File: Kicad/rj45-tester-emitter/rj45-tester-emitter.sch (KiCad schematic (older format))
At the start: 25 parts

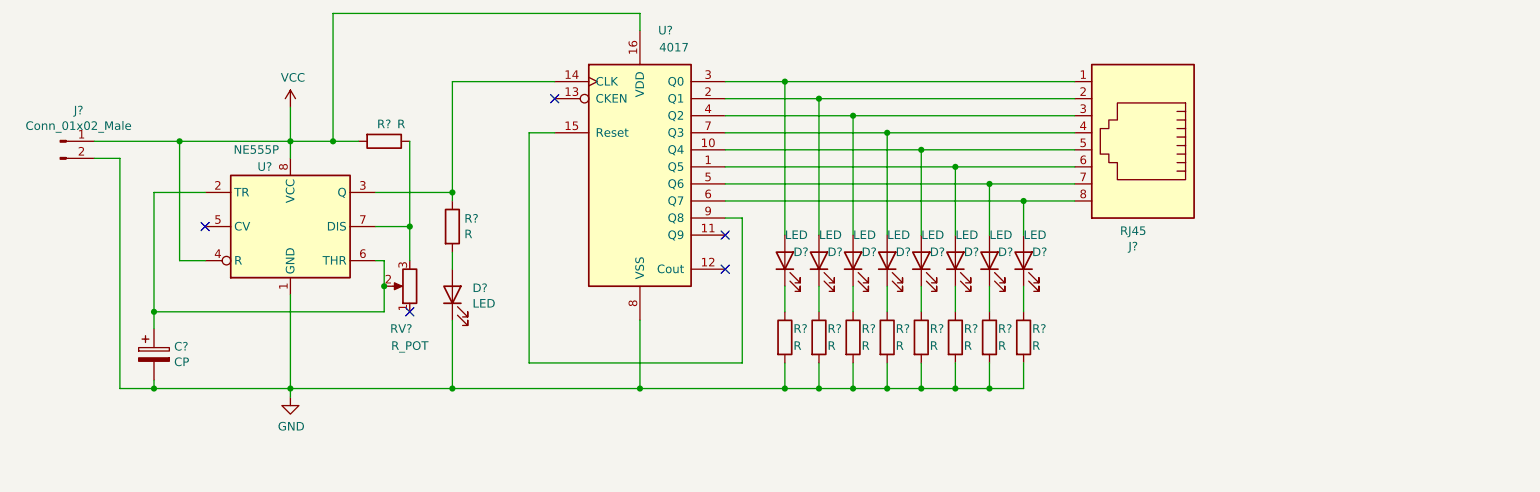
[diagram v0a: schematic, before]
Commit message: Add switch + bypass capacitor
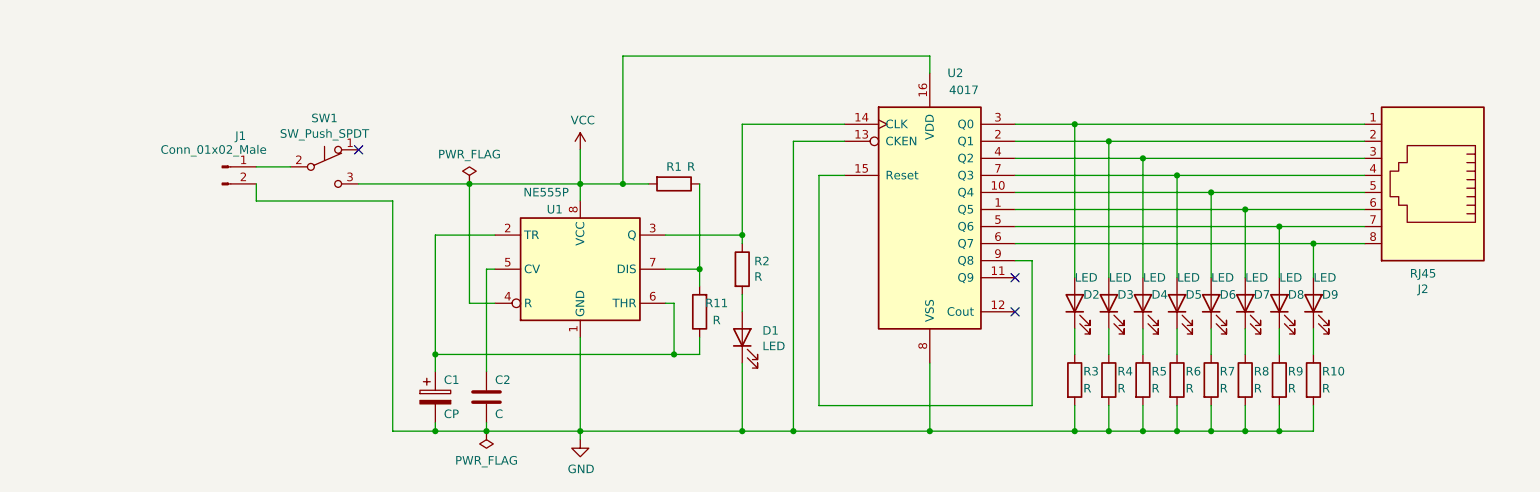
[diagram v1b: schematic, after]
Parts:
- removed RV?: R_POT, symbol Device:R_POT
- added C2: C, Capacitor_SMD:C_0805_2012Metric_Pad1.15x1.40mm_HandSolder, symbol Device:C
- added R11: R, Resistor_SMD:R_0805_2012Metric_Pad1.15x1.40mm_HandSolder, symbol Device:R
- added SW1: SW_Push_SPDT, symbol Switch:SW_Push_SPDT
- C1: renamed from C?; footprint (none) -> Capacitor_SMD:CP_Elec_6.3x5.2
- D1, D2, D3, D4, D5, D6, D7, D8, D9: renamed from D?; footprint (none) -> LED_SMD:LED_0805_2012Metric_Pad1.15x1.40mm_HandSolder
- J1: renamed from J?; footprint (none) -> Connector_JST:JST_XH_B2B-XH-A_1x02_P2.50mm_Vertical
- R1, R10, R2, R3, R4, R5, R6, R7, R8, R9: renamed from R?; footprint (none) -> Resistor_SMD:R_0805_2012Metric_Pad1.15x1.40mm_HandSolder
- U1: renamed from U?; footprint Package_DIP:DIP-8_W7.62mm -> Package_DIP:DIP-8_W8.89mm_SMDSocket_LongPads
- U2: renamed from U?; footprint (none) -> Package_DIP:DIP-16_W8.89mm_SMDSocket_LongPads
- gave numbers to parts that had none: 1
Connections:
- net GND: now also U2.13 (CKEN), C2.2
- net VCC: now also SW1.3 (C); no longer J1.1 (Pin_1)
- net at C1.1, U1.2 (TR), U1.6 (THR): now also R11.1
- net at U1.5 (CV): now also C2.1
- net at R1.1, U1.7 (DIS): now also R11.2
- new net: J1.1 (Pin_1), SW1.2 (B)
- no-connect marks 5 -> 3
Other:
- moved on the sheet: C1, D1, D2, D3, D4, D5, D6, D7, D8, D9, J1, J2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

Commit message: PCB finished
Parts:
- C1: value CP -> 47u; footprint Capacitor_SMD:CP_Elec_6.3x5.2 -> Capacitor_SMD:CP_Elec_5x5.3
- C2: value C -> 10u
- J2: footprint (none) -> Connector_RJ:RJ45_Amphenol_54602-x08_Horizontal
- R1, R11: value R -> 10K
- SW1: footprint (none) -> Connector_PinHeader_2.54mm:PinHeader_1x03_P2.54mm_Vertical
- U1: footprint Package_DIP:DIP-8_W8.89mm_SMDSocket_LongPads -> Package_SO:SOIC-8_3.9x4.9mm_P1.27mm
- U2: footprint Package_DIP:DIP-16_W8.89mm_SMDSocket_LongPads -> Package_SO:SOIC-16_3.9x9.9mm_P1.27mm
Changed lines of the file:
@@
 F 0 "U1" H 4000 3300 50  0000 C CNN
 F 1 "NE555P" H 3950 3400 50  0000 C CNN
-F 2 "Package_DIP:DIP-8_W8.89mm_SMDSocket_LongPads" H 4800 2550 50  0001 C CNN
+F 2 "Package_SO:SOIC-8_3.9x4.9mm_P1.27mm" H 4800 2550 50  0001 C CNN
 F 3 "http://www.ti.com/lit/ds/symlink/ne555.pdf" H 5000 2550 50  0001 C CNN
 	1    4150 2950
@@
 F 0 "U2" H 6350 3400 50  0000 C CNN
 F 1 "4017" H 6400 3300 50  0000 C CNN
-F 2 "Package_DIP:DIP-16_W8.89mm_SMDSocket_LongPads" H 6200 2600 50  0001 C CNN
+F 2 "Package_SO:SOIC-16_3.9x9.9mm_P1.27mm" H 6200 2600 50  0001 C CNN
 F 3 "http://www.intersil.com/content/dam/Intersil/documents/cd40/cd4017bms-22bms.pdf" H 6200 2600 50  0001 C CNN
 	1    6200 2600
@@
 $EndComp
 $Comp
-L Device:CP C1
-U 1 1 5F59578D
-P 3300 3700
-F 0 "C1" H 3350 3800 50  0000 L CNN
-F 1 "CP" H 3350 3600 50  0000 L CNN
-F 2 "Capacitor_SMD:CP_Elec_6.3x5.2" H 3338 3550 50  0001 C CNN
-F 3 "~" H 3300 3700 50  0001 C CNN
-	1    3300 3700
-	1    0    0    -1
-$EndComp
-$Comp
 L Device:LED D1
 U 1 1 5F595BD7
@@
 	0    -1   -1   0
 $EndComp
-$Comp
-L Connector:RJ45 J2
-U 1 1 5F596C3D
-P 9150 2400
-F 0 "J2" H 9207 3067 50  0000 C CNN
-F 1 "RJ45" H 9207 2976 50  0000 C CNN
-F 2 "" V 9150 2425 50  0001 C CNN
-F 3 "~" V 9150 2425 50  0001 C CNN
-	1    9150 2400
-	-1   0    0    1
-$EndComp
 Wire Wire Line
 	3650 3150 3500 3150
@@
 P 4700 2450
 F 0 "R1" V 4600 2450 50  0000 C CNN
-F 1 "R" V 4600 2550 50  0000 C CNN
+F 1 "10K" V 4600 2600 50  0000 C CNN
 F 2 "Resistor_SMD:R_0805_2012Metric_Pad1.15x1.40mm_HandSolder" V 4630 2450 50  0001 C CNN
 F 3 "~" H 4700 2450 50  0001 C CNN
@@
 P 3600 3700
 F 0 "C2" H 3650 3800 50  0000 L CNN
-F 1 "C" H 3650 3600 50  0000 L CNN
+F 1 "10u" H 3650 3600 50  0000 L CNN
 F 2 "Capacitor_SMD:C_0805_2012Metric_Pad1.15x1.40mm_HandSolder" H 3638 3550 50  0001 C CNN
 F 3 "~" H 3600 3700 50  0001 C CNN
@@
 F 0 "SW1" H 2650 2635 50  0000 C CNN
 F 1 "SW_Push_SPDT" H 2650 2544 50  0000 C CNN
-F 2 "" H 2650 2350 50  0001 C CNN
+F 2 "Connector_PinHeader_2.54mm:PinHeader_1x03_P2.54mm_Vertical" H 2650 2350 50  0001 C CNN
 F 3 "~" H 2650 2350 50  0001 C CNN
 	1    2650 2350
@@
 U 1 1 5F62B489
 P 4850 3200
-F 0 "R11" H 4750 3150 50  0000 C CNN
-F 1 "R" H 4750 3250 50  0000 C CNN
+F 0 "R11" H 4700 3150 50  0000 C CNN
+F 1 "10K" H 4700 3250 50  0000 C CNN
 F 2 "Resistor_SMD:R_0805_2012Metric_Pad1.15x1.40mm_HandSolder" V 4780 3200 50  0001 C CNN
 F 3 "~" H 4850 3200 50  0001 C CNN
@@
 	4850 3050 4850 2950
 Connection ~ 4850 2950
+$Comp
+L Connector:RJ45 J2
+U 1 1 5F5F9609
+P 9150 2400
+F 0 "J2" H 8820 2404 50  0000 R CNN
+F 1 "RJ45" H 8820 2495 50  0000 R CNN
+F 2 "Connector_RJ:RJ45_Amphenol_54602-x08_Horizontal" V 9150 2425 50  0001 C CNN
+F 3 "~" V 9150 2425 50  0001 C CNN
+	1    9150 2400
+	-1   0    0    1
+$EndComp
+$Comp
+L Device:CP C1
+U 1 1 5F59578D
+P 3300 3700
+F 0 "C1" H 3350 3800 50  0000 L CNN
+F 1 "47u" H 3350 3600 50  0000 L CNN
+F 2 "Capacitor_SMD:CP_Elec_5x5.3" H 3338 3550 50  0001 C CNN
+F 3 "~" H 3300 3700 50  0001 C CNN
+	1    3300 3700
+	1    0    0    -1
+$EndComp
 $EndSCHEMATC

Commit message: Add components values
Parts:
- R10, R2, R3, R4, R5, R6, R7, R8, R9: value R -> 150R
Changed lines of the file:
@@
 P 5100 2950
 F 0 "R2" H 5170 2996 50  0000 L CNN
-F 1 "R" H 5170 2905 50  0000 L CNN
+F 1 "150R" H 5170 2905 50  0000 L CNN
 F 2 "Resistor_SMD:R_0805_2012Metric_Pad1.15x1.40mm_HandSolder" V 5030 2950 50  0001 C CNN
 F 3 "~" H 5100 2950 50  0001 C CNN
@@
 U 1 1 5F5AD454
 P 7050 3600
-F 0 "R3" H 7100 3650 50  0000 L CNN
-F 1 "R" H 7100 3550 50  0000 L CNN
+F 0 "R3" V 6950 3400 50  0000 L CNN
+F 1 "150R" V 6950 3550 50  0000 L CNN
 F 2 "Resistor_SMD:R_0805_2012Metric_Pad1.15x1.40mm_HandSolder" V 6980 3600 50  0001 C CNN
 F 3 "~" H 7050 3600 50  0001 C CNN
@@
 U 1 1 5F5AD7C2
 P 7250 3600
-F 0 "R4" H 7300 3650 50  0000 L CNN
-F 1 "R" H 7300 3550 50  0000 L CNN
+F 0 "R4" V 7150 3400 50  0000 L CNN
+F 1 "150R" V 7150 3550 50  0000 L CNN
 F 2 "Resistor_SMD:R_0805_2012Metric_Pad1.15x1.40mm_HandSolder" V 7180 3600 50  0001 C CNN
 F 3 "~" H 7250 3600 50  0001 C CNN
@@
 U 1 1 5F5AD97F
 P 7450 3600
-F 0 "R5" H 7500 3650 50  0000 L CNN
-F 1 "R" H 7500 3550 50  0000 L CNN
+F 0 "R5" V 7350 3400 50  0000 L CNN
+F 1 "150R" V 7350 3550 50  0000 L CNN
 F 2 "Resistor_SMD:R_0805_2012Metric_Pad1.15x1.40mm_HandSolder" V 7380 3600 50  0001 C CNN
 F 3 "~" H 7450 3600 50  0001 C CNN
@@
 U 1 1 5F5ADB22
 P 7650 3600
-F 0 "R6" H 7700 3650 50  0000 L CNN
-F 1 "R" H 7700 3550 50  0000 L CNN
+F 0 "R6" V 7550 3400 50  0000 L CNN
+F 1 "150R" V 7550 3550 50  0000 L CNN
 F 2 "Resistor_SMD:R_0805_2012Metric_Pad1.15x1.40mm_HandSolder" V 7580 3600 50  0001 C CNN
 F 3 "~" H 7650 3600 50  0001 C CNN
@@
 U 1 1 5F5ADC51
 P 7850 3600
-F 0 "R7" H 7900 3650 50  0000 L CNN
-F 1 "R" H 7900 3550 50  0000 L CNN
+F 0 "R7" V 7750 3400 50  0000 L CNN
+F 1 "150R" V 7750 3550 50  0000 L CNN
 F 2 "Resistor_SMD:R_0805_2012Metric_Pad1.15x1.40mm_HandSolder" V 7780 3600 50  0001 C CNN
 F 3 "~" H 7850 3600 50  0001 C CNN
@@
 U 1 1 5F5ADDFA
 P 8050 3600
-F 0 "R8" H 8100 3650 50  0000 L CNN
-F 1 "R" H 8100 3550 50  0000 L CNN
+F 0 "R8" V 7950 3400 50  0000 L CNN
+F 1 "150R" V 7950 3550 50  0000 L CNN
 F 2 "Resistor_SMD:R_0805_2012Metric_Pad1.15x1.40mm_HandSolder" V 7980 3600 50  0001 C CNN
 F 3 "~" H 8050 3600 50  0001 C CNN
@@
 U 1 1 5F5ADF9C
 P 8250 3600
-F 0 "R9" H 8300 3650 50  0000 L CNN
-F 1 "R" H 8300 3550 50  0000 L CNN
+F 0 "R9" V 8150 3400 50  0000 L CNN
+F 1 "150R" V 8150 3550 50  0000 L CNN
 F 2 "Resistor_SMD:R_0805_2012Metric_Pad1.15x1.40mm_HandSolder" V 8180 3600 50  0001 C CNN
 F 3 "~" H 8250 3600 50  0001 C CNN
@@
 U 1 1 5F5AE091
 P 8450 3600
-F 0 "R10" H 8500 3650 50  0000 L CNN
-F 1 "R" H 8500 3550 50  0000 L CNN
+F 0 "R10" V 8350 3350 50  0000 L CNN
+F 1 "150R" V 8350 3550 50  0000 L CNN
 F 2 "Resistor_SMD:R_0805_2012Metric_Pad1.15x1.40mm_HandSolder" V 8380 3600 50  0001 C CNN
 F 3 "~" H 8450 3600 50  0001 C CNN
